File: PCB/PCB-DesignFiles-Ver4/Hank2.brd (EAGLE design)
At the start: 168.9 x 119.4 mm, 118 parts, among them T1 2n2222, T2 2n2222, T3 2n2222, T4 2n2222, T5 2n2222, T6 2n2222, T7 2n2222, T8 2n2222

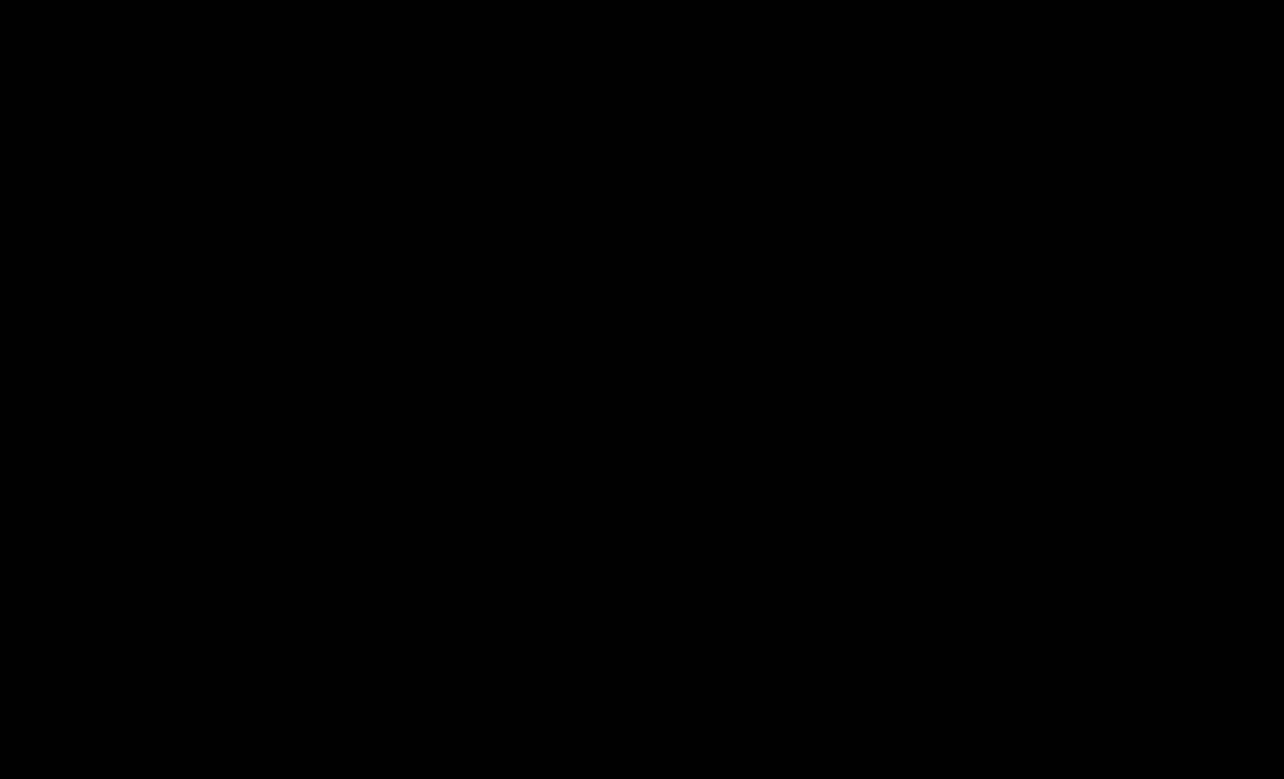
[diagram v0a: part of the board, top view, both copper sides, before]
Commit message: Added ESP32Dev Kit library to PCB
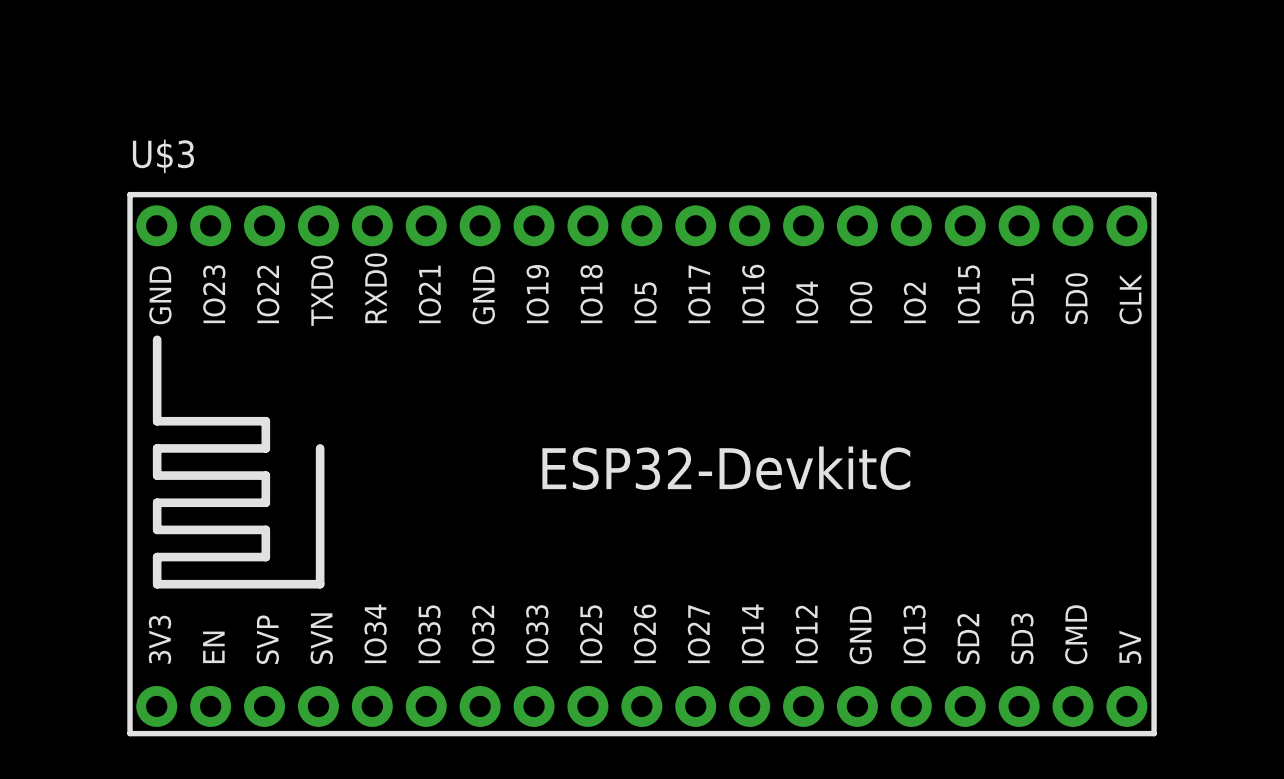
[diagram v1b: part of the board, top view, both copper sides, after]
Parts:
- added U$3: ESP32DEVKITC, ESP32-DEVKITC:ESP32-DEVKITC
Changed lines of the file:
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@@
 <element name="PR_5V2" library="rcl" package="0207/10" value="1k" x="6.985" y="-46.99"/>
 <element name="U$2" library="HankLibrariesV2" package="BLUETOOTH_FOOTPRINT" value="BLUETOOTH" x="65.405" y="-41.275" rot="R180"/>
+<element name="U$3" library="ESP32-DEVKITC" package="ESP32-DEVKITC" value="ESP32DEVKITC" x="28.575" y="-75.565"/>
 </elements>
 <signals>

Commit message: Mods added to pcb finished, now route the PCB
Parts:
- removed BREAKOUT: (no value), con-lstb:MA10-2
- removed C_OLED: 0.1uF, rcl:C025-024X044
- removed JTAG: (no value), con-lstb:MA03-2
- removed J_3V3V: Jumper, con-molex:22-23-2021
- removed LED1, LED2: (no value), led:LED3MM
- removed PR_5V1, PR_5V2, R_NI1, R_UTX1: 1k, rcl:0207/10
- removed R_NI2, R_UTX2: 2K, rcl:0207/10
- removed SSR1, SSR2, SSR3, SSR4, SSR5, SSR6, SSR7, SSR8: SSR, HankLibraries:SSR_FOOTPRINT
- removed U$7: SD_CARD_READER, HankLibraries:SD_CARD_READER_FOOTPRINT
- added ASC: LM358, SparkFun-IC-Amplifiers:DIP08
- added C_RTC1: 0.1uF, rcl:C025-024X044
- added I2CR1, I2CR2: 4.7K, rcl:0207/10
- added I2C_BUS: (no value), con-lstb:MA04-1
- added LS11, LS12, LS21, LS22, LS31, LS32: 10K, rcl:0207/10
- added LSQ1, LSQ2, LSQ3: BSS138, adafruit:SOT23
- added SA1, SA2: 1k, rcl:0207/10
- added SAD1, SAD2: (no value), led:LED3MM
- added SC11: 51.5K, rcl:0207/10
- added SC12, SC22: 100k, rcl:0207/10
- added SC21: 51k1, rcl:0207/10
- added SV2, SV3: (no value), con-lstb:MA03-1
- added U$10, U$11, U$12, U$13, U$5, U$8, U$9: SSR, HankLibrariesV2:SSR_FOOTPRINT
- added U$14: MA19-1, con-lstb:MA19-1
- added U$15: SD_CARD_READER, HankLibrariesV2:SD_CARD_READER_FOOTPRINT
- RO12: value 150 -> 10k
- RO22, RO32, RO42, RO62, RO72, RO82: value 150 -> 10K
- U$1: value FLASH_MEMORY -> MA19-1; device HankLibraries:FLASHMEMORY_FOOTPRINT -> con-lstb:MA19-1
- U$4: value BLUETOOTH -> SSR; device HankLibraries:BLUETOOTH_FOOTPRINT -> HankLibrariesV2:SSR_FOOTPRINT
- moved U$3 136.6 mm to (25.4, 61.0), turned to 180 degrees
- moved U$2 134.2 mm to (20.3, 85.1)
- moved U$4 121.2 mm to (137.8, 55.2), turned to 0 degrees
- moved U$1 76.7 mm to (26.0, 76.2)
- moved FUSE6 3.42 mm to (148.3, 92.1)
- moved FUSE5 0.90 mm to (148.0, 103.5)
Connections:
- removed net FLASH_CLK: BREAKOUT.4, U$1.CLK
- removed net FLASH_CS: BREAKOUT.2, U$1.CS
- removed net FLASH_DI: BREAKOUT.6, U$1.DI
- removed net FLASH_DO: BREAKOUT.8, U$1.DO
- removed net N$1: BREAKOUT.1, J_5V.2
- removed net N$2: BREAKOUT.3, J_3V3V.2
- removed net N$39: IO_UC.16, R_NI1.2
- removed net NEW_IN: BREAKOUT.11, R_NI1.1, R_NI2.1
- removed net U_TX_3: BREAKOUT.15, R_UTX1.1, R_UTX2.2
- new net 3V3_OUT_ESP32: U$1.19, U$3.1
- new net 5V_BOARD: J_5V.2, U$1.1, U$3.19
- new net EN_ESP32: U$1.18, U$3.2
- new net L_AUTOMANUAL: LS31.1, LSQ3.2, U$1.9, U$3.11
- new net L_URX: LS11.1, LSQ1.2, U$14.9, U$3.28
- new net L_UTX: LS21.1, LSQ2.2, U$14.8, U$3.27
- new net N$38: SC21.2, SV2.3
- new net N$43: ASC.5, SC11.1, SC12.2
- new net N$44: ASC.3, SC21.1, SC22.2
- new net N$47: SC11.2, SV3.3
- new net PRESS_SEN1: ASC.6, ASC.7, U$1.17, U$3.3
- new net PRESS_SEN2: ASC.1, ASC.2, U$1.16, U$3.4
- new net SPARE_IO0: U$14.6, U$3.25
- new net SPARE_IO1: U$14.16, U$3.35
- new net SPARE_IO10: U$1.3, U$3.17
- new net SPARE_IO11: U$1.2, U$3.18
- new net SPARE_IO12: U$1.7, U$3.13
- new net SPARE_IO13: U$1.5, U$3.15
- new net SPARE_IO14: U$1.8, U$3.12
- new net SPARE_IO15: U$14.4, U$3.23
- new net SPARE_IO2: U$14.5, U$3.24
- new net SPARE_IO3: U$14.15, U$3.34
- new net SPARE_IO34: U$1.15, U$3.5
- new net SPARE_IO35: U$1.14, U$3.6
- new net SPARE_IO6: U$14.1, U$3.20
- new net SPARE_IO7: U$14.2, U$3.21
- new net SPARE_IO8: U$14.3, U$3.22
- new net SPARE_IO9: U$1.4, U$3.16
- new net U_SPARE: IO_UC.16
- net +3V3: now also C_RTC1.1, I2CR1.2, I2CR2.2, I2C_BUS.3, LS11.2, LS21.2, LS31.2, LSQ1.1, LSQ2.1, LSQ3.1, U$2.+3.3; no longer C_OLED.1, C_USD.1, J_3V3V.1, U$1.HOLD, U$1.VCC, U$1.WP, U$4.+3.3, U$7.+3.3
- net +5V: now also ASC.8, C_USD.1, LS12.2, LS22.2, LS32.2, SV2.2, SV3.2, U$10.3, U$11.3, U$12.3, U$13.3, U$15.+5V, U$4.3, U$5.3, U$8.3, U$9.3; no longer JTAG.2, SSR1.3, SSR2.3, SSR3.3, SSR4.3, SSR5.3, SSR6.3, SSR7.3, SSR8.3
- net AUTO_MANUAL: now also LS32.1, LSQ3.3; no longer BREAKOUT.20, JTAG.4
- net BT_RX: now also U$14.7, U$2.RXD, U$3.26; no longer BREAKOUT.7, U$4.RXD
- net BT_TX: now also U$1.11, U$2.TXD, U$3.9; no longer BREAKOUT.9, U$4.TXD
- net GND: now also ASC.4, C_RTC1.2, I2C_BUS.4, SA1.1, SA2.1, SC12.1, SC22.1, SV2.1, SV3.1, U$1.6, U$14.13, U$14.19, U$15.GND, U$2.GND, U$3.14, U$3.32, U$3.38; no longer BREAKOUT.5, C_OLED.2, JTAG.6, PR_5V1.1, PR_5V2.1, R_NI2.2, R_UTX2.1, U$1.GND, U$4.GND, U$7.GND
- net IN7: no longer JTAG.1
- net IN8: no longer JTAG.3
- net L1-1: now also U$10.1, U$4.1, U$5.1, U$8.1; no longer SSR1.1, SSR2.1, SSR3.1, SSR4.1
- net L1-2: now also U$11.1, U$12.1, U$13.1, U$9.1; no longer SSR5.1, SSR6.1, SSR7.1, SSR8.1
- net LED2: now also SA2.2, SAD2.K; no longer LED2.K, PR_5V2.2
- net L_O1: now also U$8.4; no longer SSR2.4
- net L_O3: now also U$5.4; no longer SSR3.4
- net MISO: now also U$14.12, U$15.MISO, U$3.31; no longer BREAKOUT.10, U$7.MISO
- net MOSI: now also U$14.18, U$15.MOSI, U$3.37; no longer BREAKOUT.12, U$7.MOSI
- net N$10: now also U$13.2; no longer SSR8.2
- net N$12: now also U$9.4; no longer SSR5.4
- net N$13: now also U$12.2; no longer SSR7.2
- net N$14: now also U$8.2; no longer SSR2.2
- net N$15: now also U$5.2; no longer SSR3.2
- net N$17: now also U$11.4; no longer SSR6.4
- net N$19: now also U$11.2; no longer SSR6.2
- net N$21: now also U$12.4; no longer SSR7.4
- net N$24: now also U$10.2; no longer SSR4.2
- net N$26: now also U$13.4; no longer SSR8.4
- net N$28: now also U$9.2; no longer SSR5.2
- net N$3: now also U$4.2; no longer SSR1.2
- net N$30: now also U$4.4; no longer SSR1.4
- net N$42: now also U$10.4; no longer SSR4.4
- net N$6: now also SA1.2, SAD1.K; no longer LED1.K, PR_5V1.2
- net SCK: now also U$14.11, U$15.SCK, U$3.30; no longer BREAKOUT.14, U$7.SCK
- net SCL: now also I2CR1.1, I2C_BUS.1, U$14.17, U$3.36; no longer BREAKOUT.19
- net SDA: now also I2CR2.1, I2C_BUS.2, U$14.14, U$3.33; no longer BREAKOUT.17
- net SD_CS: now also U$14.10, U$15.CS, U$3.29; no longer BREAKOUT.16, U$7.CS
- net STAY_ALIVE1: now also SAD1.A, U$1.13, U$3.7; no longer LED1.A
- net STAY_ALIVE2: now also SAD2.A, U$1.12, U$3.8; no longer LED2.A
- net TEMP_SEN: now also U$1.10, U$3.10; no longer BREAKOUT.18
- net U_RESET: no longer JTAG.5
- net U_RX: now also LS12.1, LSQ1.3; no longer BREAKOUT.13
- net U_TX: now also LS22.1, LSQ2.3; no longer R_UTX1.2
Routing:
- net FLASH_CS: track 154.7 -> 0.00 mm
- net FLASH_CLK: track 148.2 -> 0.00 mm
- net FLASH_DI: track 141.9 -> 0.00 mm
- net FLASH_DO: track 135.7 -> 0.00 mm
- net +5V: track 454.4 -> 353.6 mm
- net SCK: track 100.3 -> 0.00 mm
- net +3V3: track 257.5 -> 164.1 mm
- net NEW_IN: track 92.9 -> 0.00 mm, vias 1 -> 0
- net MOSI: track 85.0 -> 0.00 mm, vias 3 -> 0
- net SD_CS: track 84.9 -> 0.00 mm
- net MISO: track 74.7 -> 0.00 mm, vias 2 -> 0
- net L1-1: track 85.6 -> 31.7 mm
- net L1-2: track 56.1 -> 7.84 mm
- net BT_RX: track 39.2 -> 0.00 mm, vias 1 -> 0
- net BT_TX: track 39.2 -> 0.00 mm, vias 1 -> 0
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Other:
- board text removed: "INT1"

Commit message: Changes to the transistorss footprint, ready to route
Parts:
- removed T1, T2, T3, T4, T5, T6, T7, T8: 2n2222, transistor:TO92-ECB
- added 2N2222_1, 2N2222_2, 2N2222_3, 2N2222_4, 2N2222_5, 2N2222_6, 2N2222_7, 2N2222_8: (no value), transistor:TO92-EBC
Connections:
- removed net N$17: LO6.K, T6.C, U$11.4
- removed net N$34: RO82.1, T8.B
- new net 2N2222_6: 2N2222_6.C, LO6.K, U$11.4
- new net N$2: 2N2222_1.B, RO12.1
- net GND: now also 2N2222_1.E, 2N2222_2.E, 2N2222_3.E, 2N2222_4.E, 2N2222_5.E, 2N2222_6.E, 2N2222_7.E, 2N2222_8.E; no longer T1.E, T2.E, T3.E, T4.E, T5.E, T6.E, T7.E, T8.E
- net L_O1: now also 2N2222_2.C; no longer T2.C
- net L_O3: now also 2N2222_3.C; no longer T3.C
- net N$12: now also 2N2222_5.C; no longer T5.C
- net N$18: now also 2N2222_2.B, RO22.1; no longer RO62.1, T6.B
- net N$21: now also 2N2222_7.C; no longer T7.C
- net N$22: now also 2N2222_7.B; no longer T7.B
- net N$23: now also 2N2222_3.B, RO32.1; no longer RO42.1, T4.B
- net N$26: now also 2N2222_8.C; no longer T8.C
- net N$27: now also 2N2222_4.B, RO42.1; no longer RO32.1, T3.B
- net N$30: now also 2N2222_1.C; no longer T1.C
- net N$31: now also 2N2222_8.B, RO82.1; no longer RO22.1, T2.B
- net N$42: now also 2N2222_4.C; no longer T4.C
- net N$8: now also 2N2222_5.B, RO52.1; no longer RO12.1, T1.B
- net N$9: now also 2N2222_6.B, RO62.1; no longer RO52.1, T5.B
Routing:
- net N$17: track 11.2 -> 0.00 mm
- net 2N2222_6: track 0.00 -> 8.89 mm
- net N$31: track 6.86 -> 0.00 mm
- net N$23: track 6.66 -> 0.00 mm
- net N$27: track 6.21 -> 0.00 mm
- net N$18: track 5.61 -> 0.00 mm
- net N$9: track 5.08 -> 0.00 mm
- net N$8: track 5.08 -> 0.00 mm
- net N$34: track 5.08 -> 0.00 mm
- net N$22: track 5.08 -> 0.00 mm
- net N$42: track 11.0 -> 7.62 mm
- net L_O3: track 10.9 -> 7.62 mm
- net N$30: track 11.2 -> 8.89 mm
- net N$26: track 11.2 -> 8.89 mm
- net N$21: track 11.2 -> 8.89 mm
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
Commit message: routing
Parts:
- moved 2N2222_8 302.0 mm to (113.7, 71.1)
- moved 2N2222_7 285.2 mm to (116.8, 82.5), turned to 90 degrees
- moved 2N2222_5 282.7 mm to (118.7, 114.9)
- moved 2N2222_6 280.1 mm to (117.5, 99.7)
- moved 2N2222_4 259.6 mm to (118.1, 15.9)
- moved 2N2222_3 257.2 mm to (115.6, 27.9)
- moved 2N2222_2 251.7 mm to (117.5, 41.3)
- moved ASC 159.9 mm to (74.9, 142.9)
- moved SC11 159.9 mm to (90.8, 132.7)
- moved SC12 159.9 mm to (90.8, 128.9)
- moved SC21 159.9 mm to (76.2, 128.3)
- moved SC22 159.9 mm to (76.2, 132.1)
- moved SV2 159.9 mm to (63.5, 130.2)
- moved SV3 159.9 mm to (62.2, 141.6)
- moved SKT1 1.91 mm to (165.1, 30.5)
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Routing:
- net MO1: track 13.9 -> 15.8 mm
- net MO6: track 8.60 -> 10.5 mm
- net MO7: track 19.1 -> 21.0 mm
- net MO5: track 8.97 -> 10.9 mm
- net MO3: track 13.0 -> 14.9 mm
- net L1-2: track 7.84 -> 9.73 mm
- net MO2: track 7.73 -> 9.61 mm
- net MO4: track 18.3 -> 19.3 mm
- net L1-1: track 31.7 -> 32.7 mm

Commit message: Mods to PCB
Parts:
- moved I2C_BUS 161.7 mm to (81.9, 114.9), turned to 180 degrees
- moved I2CR2 154.8 mm to (81.3, 109.2), turned to 180 degrees
- moved I2CR1 149.6 mm to (81.3, 105.4), turned to 180 degrees
- moved OLED_DISPLAY 32.8 mm to (67.3, 114.9), turned to 180 degrees
- moved J_5V 27.3 mm to (56.5, 69.2)
- moved U$8 19.1 mm to (144.1, 39.4)
- moved FTDI 18.5 mm to (89.5, 9.53)
- moved U$10 17.2 mm to (144.1, 11.4)
- moved U$13 16.6 mm to (143.5, 67.9)
- moved U$5 16.2 mm to (144.1, 25.4)
- moved C_BT 16.1 mm to (25.4, 85.1)
- moved C_UXTAL1 14.7 mm to (59.1, 39.4)
- moved C_UXTAL2 14.6 mm to (55.9, 39.4)
- moved TEMP_SENSOR 13.2 mm to (54.6, 114.9), turned to 180 degrees
- moved C_USD 11.4 mm to (29.2, 113.0)
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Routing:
- net +5V: track 353.6 -> 509.2 mm
- net U_RESET: track 76.7 -> 203.3 mm
- net SCL: track 29.3 -> 104.8 mm, vias 2 -> 1
- net SDA: track 60.8 -> 124.4 mm
- net OUT3: track 46.8 -> 110.2 mm
- net RTS: track 15.2 -> 72.8 mm
- net OUT1: track 49.9 -> 104.5 mm
- net OUT2: track 40.1 -> 93.8 mm
- net AUTO_MANUAL: track 117.4 -> 167.4 mm
- net +3V3: track 164.1 -> 213.1 mm, vias 1 -> 0
- net CP12: track 43.9 -> 77.5 mm
- net 5V_BOARD: track 2.29 -> 29.6 mm
- net GND: track 24.0 -> 45.8 mm
- net UTX: track 29.7 -> 46.8 mm
- net N$4: track 4.86 -> 18.0 mm
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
